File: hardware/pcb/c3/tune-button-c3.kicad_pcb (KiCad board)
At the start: 2 copper layers, 46 x 70 mm, 42 parts, among them J1 USB-C, J2 LiPo, Q1 AO3401A, SW1 MX switch, SW2 MX switch, SW3 MX switch, SW4 MX switch, SW5 RESET, SW6 BOOT, U1 ESP32-C3-WROOM-02-N4, U2 SRV05-4, U3 TP4054, U4 RT9080-3.3

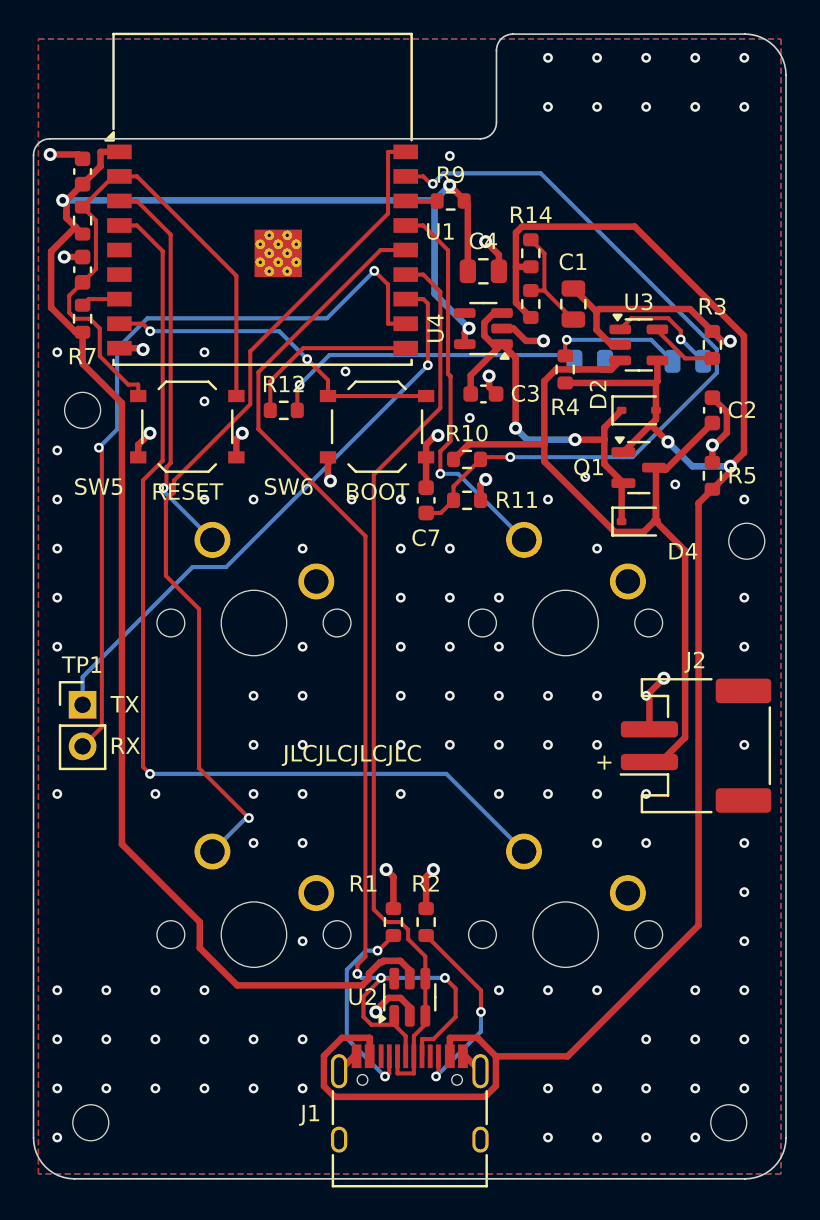
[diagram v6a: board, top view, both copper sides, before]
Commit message: pcb: fixes from the fourth simulation pass
- C3: R13/R14 (plug-in damping) are 1206, not 0603. Each takes a ~35 W,
  ~50 uJ pulse per plug-in from a stiff source, about twice an 0603's
  repetitive pulse rating. Moved flat above U4; C1 nudged down.
- XIAO: D1 is a 1N4148WS, not a BAT54W. A Schottky's reverse leakage
  dragged K4 low while K3 was held, from about 60 C.
- R5 comment: the unplug gap is 5-8 ms, up to ~15 ms at tolerance extremes.
- wiring.md: the divider holds GPIO2 below the high threshold; it doesn't
  select the boot mode on the C3, so that is fine.
- README: the firmware pin map doesn't match either board yet, and a low
  cell sags the C3 rail on Wi-Fi-sized bursts.
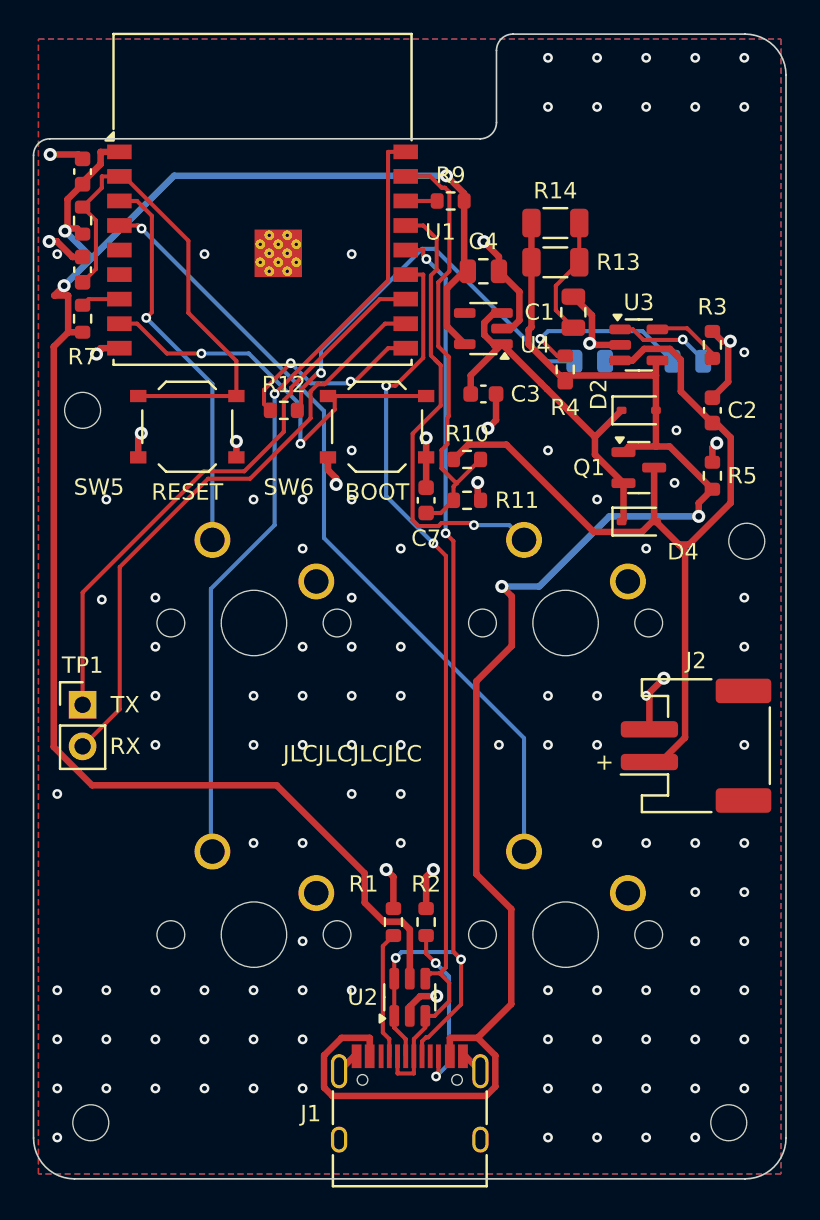
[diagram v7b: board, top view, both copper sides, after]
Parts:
- R13, R14: footprint Resistor_SMD:R_0603_1608Metric -> Resistor_SMD:R_1206_3216Metric
- moved R13 2.96 mm to (31.9, 13.9), turned to 0 degrees
- moved R14 2.38 mm to (31.9, 11.6), turned to 0 degrees
- moved C1 0.50 mm to (33.0, 17.0)
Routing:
- net VBAT_SENSE: track 47.2 -> 27.2 mm, vias 2 -> 0
- net VBUS: track 117.6 -> 98.3 mm
- net K3: track 60.8 -> 49.2 mm
- net RXD: track 47.7 -> 36.5 mm, vias 2 -> 0
- net USB_DP: track 72.0 -> 63.0 mm, vias 3 -> 4
- net LED_A: track 19.3 -> 25.3 mm
- net CC1: track 12.6 -> 7.81 mm, vias 2 -> 0
- net K4: track 52.6 -> 48.4 mm
- net IO9: track 21.2 -> 25.3 mm
- net K1: track 24.2 -> 28.3 mm
- net EN: track 35.2 -> 31.3 mm
- net GND: track 55.1 -> 51.2 mm, vias 126 -> 123
- net VBAT: track 50.5 -> 53.9 mm
- net CHG_A: track 8.04 -> 11.0 mm
- net VSYS: track 26.1 -> 23.5 mm, vias 2 -> 0
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
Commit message: pcb: fixes from the fifth audit
- XIAO D1: LCSC C2128 (Changjing 1N4148WS, Basic), so it appears in the JLC
  BOM/CPL. Its VF max of 0.715 V at 1 mA is what the K4 press needs to read
  low at -20 C; the README says so. Hand-soldering footprint, as that board is.
- Labels: a label must be nearer its own part than any other by 0.25 mm,
  measured edge to edge (it was centre to body). C1's label passes that and
  stays beside C1; U4's, which the first try at this rule hid, is placed.
- route.py drops exactly repeated track segments from the saved board
  (removing them through pcbnew's bindings crashes it later in the run).
- variant_xiao docstring no longer says Schottky.
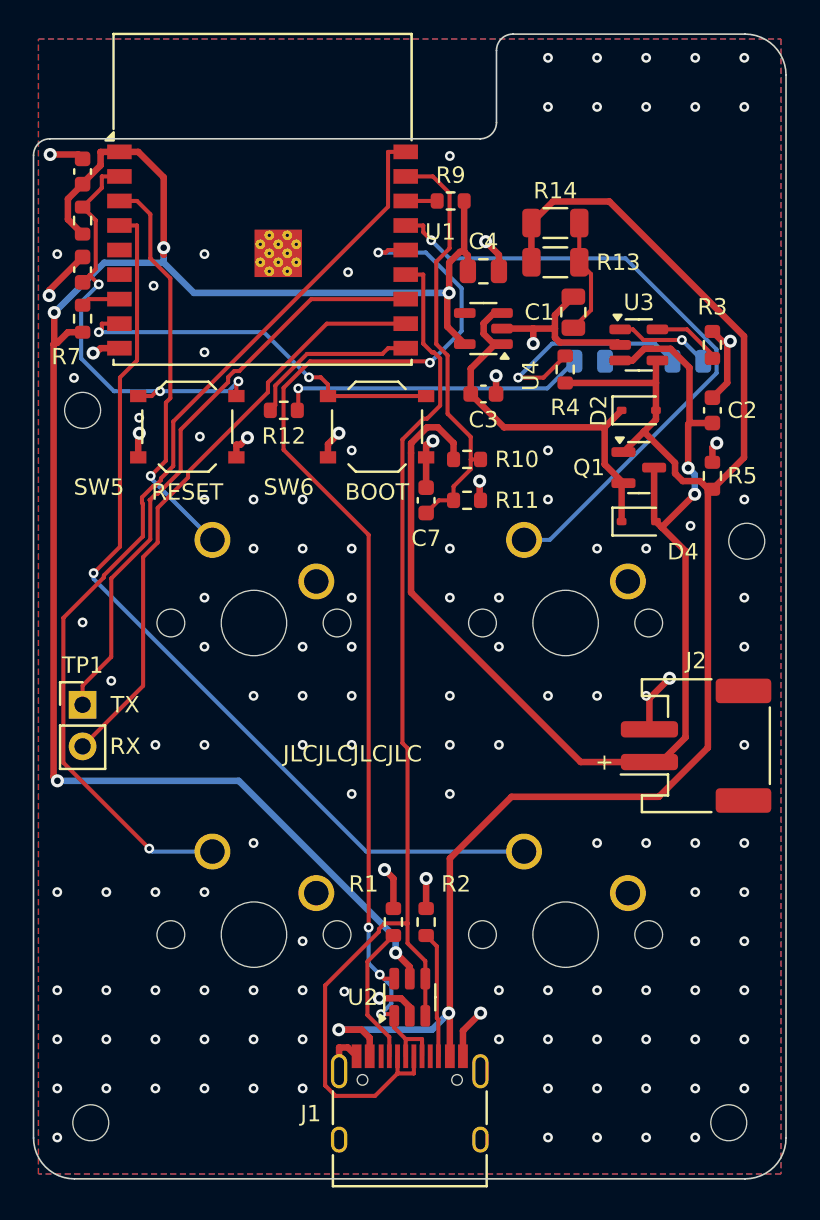
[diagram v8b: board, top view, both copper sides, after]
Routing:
- net VBAT: track 53.9 -> 69.7 mm, vias 0 -> 2
- net USB_DN: track 57.4 -> 69.7 mm, vias 2 -> 0
- net K1: track 28.3 -> 39.8 mm
- net K4: track 48.4 -> 58.1 mm
- net K3: track 49.2 -> 57.0 mm
- net USB_DP: track 63.0 -> 70.7 mm, vias 4 -> 5
- net LED_A: track 25.3 -> 18.9 mm
- net VBUS: track 98.3 -> 104.5 mm
- net EN: track 31.3 -> 27.6 mm, vias 0 -> 3
- net 3V3: track 109.3 -> 112.7 mm, vias 3 -> 5
- net CHG_A: track 11.0 -> 14.2 mm
- net GND: track 51.2 -> 54.4 mm, vias 123 -> 134
- net CC2: track 10.8 -> 7.69 mm, vias 2 -> 0
- net LED: track 12.1 -> 10.6 mm, vias 2 -> 0
- net IO9: track 25.3 -> 23.7 mm
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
